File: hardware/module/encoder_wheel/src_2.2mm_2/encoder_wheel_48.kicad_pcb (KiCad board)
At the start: 2 copper layers, 74 x 74 mm, 2 parts

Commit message: encoder changes
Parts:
- renumbered REF** to ENC1, REF** to ENC2

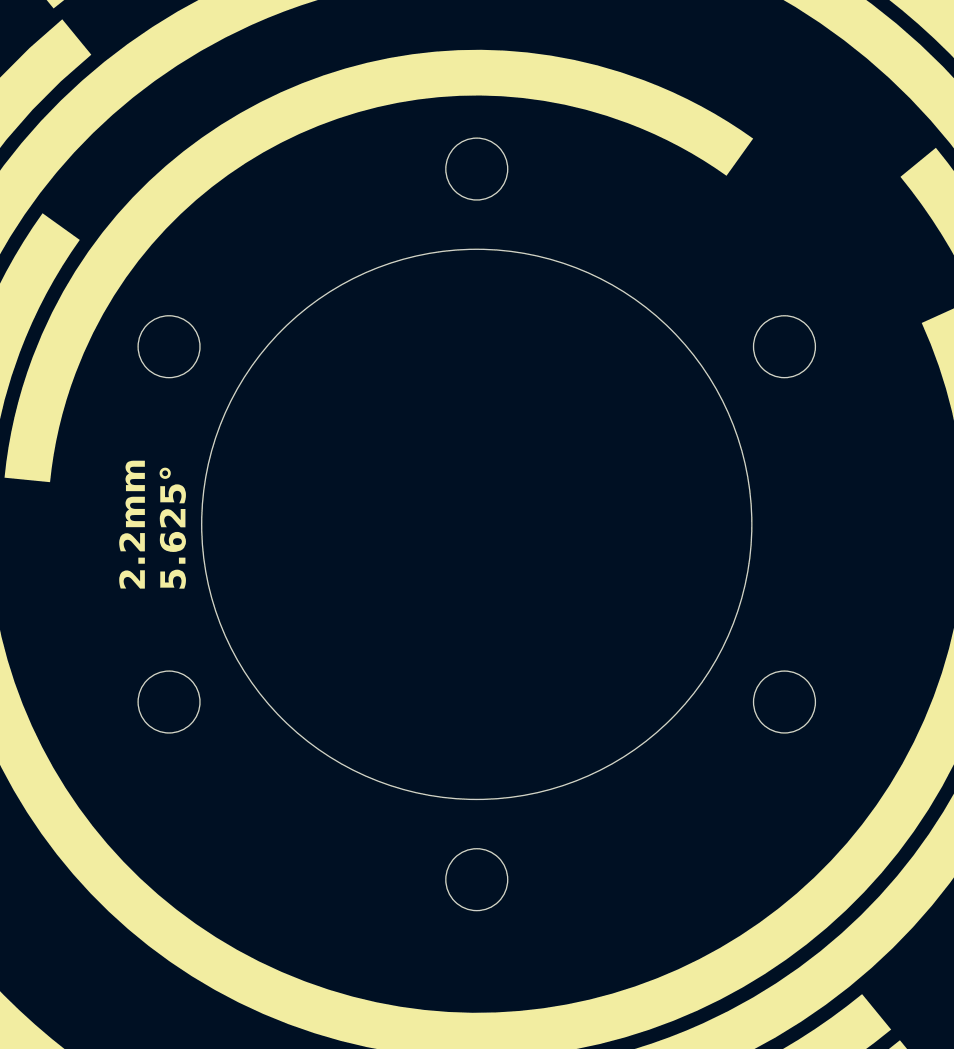
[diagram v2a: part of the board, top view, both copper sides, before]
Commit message: changed hole patern encoder wheel
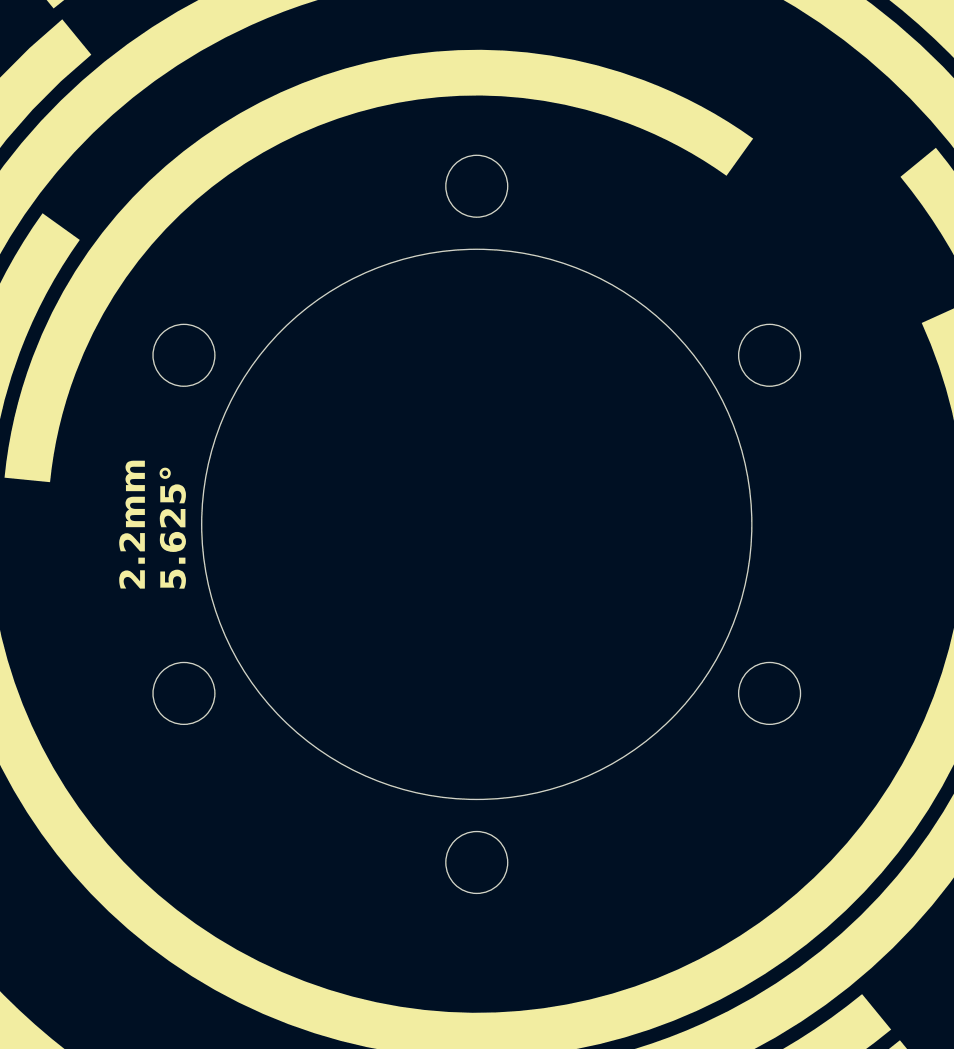
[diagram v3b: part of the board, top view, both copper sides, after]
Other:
- outline, holes or cut-outs redrawn
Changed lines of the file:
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@@
 				(xy 15.411921 -29.970747) (xy 15.898127 -29.716055) (xy 16.378717 -29.454359) (xy 16.853678 -29.185778)
 				(xy 15.852625 -27.453656) (xy 15.405903 -27.705999) (xy 14.953888 -27.951905) (xy 14.496592 -28.191261)
-				(xy 14.034024 -28.423958) (xy 13.566196 -28.649886) (xy 13.093119 -28.868934) (xy 12.6148 -29.080992)
+				(xy 14.034024 -28.423958) (xy 13.566196 -28.649886) (xy 13.093119 -28.868934) (xy 12.614798 -29.080992)
 				(xy 12.131258 -29.28595) (xy 11.645881 -29.482376) (xy 11.159155 -29.670143) (xy 10.671175 -29.849318)
 				(xy 10.182037 -30.019967) (xy 9.691836 -30.182158) (xy 9.200669 -30.335958) (xy 8.708632 -30.481435)
@@
 				(xy 5.848459 25.233587) (xy 5.027658 25.410212) (xy 4.205519 25.559396) (xy 3.382624 25.681424)
 				(xy 3.121843 23.700253) (xy 3.880692 23.587004) (xy 4.638938 23.448764) (xy 5.396048 23.285271)
-				(xy 6.15149 23.096262) (xy 6.904733 22.881472) (xy 7.655243 22.640638) (xy 8.402493 22.373497) (xy 9.145941 22.079785)
+				(xy 6.15149 23.096262) (xy 6.904733 22.881472) (xy 7.655243 22.640638) (xy 8.402495 22.373497) (xy 9.145941 22.079785)
 				(xy 10.271285 21.58003) (xy 11.358193 21.030029) (xy 12.405858 20.431736) (xy 13.413469 19.787104)
 				(xy 14.380217 19.098086) (xy 15.305294 18.366635) (xy 16.187891 17.594705) (xy 17.027198 16.784249)
@@
 				(xy -22.883793 -4.400149) (xy -22.634455 -5.538097) (xy -22.325558 -6.67145) (xy -21.956306 -7.798286)
 				(xy -21.525904 -8.916684) (xy -21.215974 -9.631281) (xy -20.884991 -10.330217) (xy -20.533501 -11.013306)
-				(xy -20.162047 -11.680366) (xy -19.771177 -12.3312) (xy -19.361434 -12.965632) (xy -18.933364 -13.583472)
+				(xy -20.162047 -11.680367) (xy -19.771177 -12.3312) (xy -19.361434 -12.965632) (xy -18.933364 -13.583472)
 				(xy -18.487513 -14.184533)
 			)
@@
 		(fp_poly
 			(pts
-				(xy 32.816366 7.646893) (xy 33.049092 6.574799) (xy 33.247099 5.49443) (xy 33.41003 4.406632) (xy 33.53754 3.312247)
+				(xy 32.816366 7.646893) (xy 33.04909 6.574799) (xy 33.247099 5.49443) (xy 33.41003 4.406632) (xy 33.53754 3.312247)
 				(xy 33.629279 2.212122) (xy 33.6849 1.107101) (xy 33.704054 -0.001973) (xy 31.709173 -0.001256)
 				(xy 31.691908 1.042432) (xy 31.640268 2.082254) (xy 31.554595 3.117414) (xy 31.43522 4.147115) (xy 31.282476 5.170561)
@@
 				(xy -15.850977 27.457433) (xy -16.735616 26.928095) (xy -17.171709 26.652536) (xy -17.603515 26.369771)
 				(xy -18.030934 26.07984) (xy -18.453864 25.782782) (xy -18.872208 25.478638) (xy -19.285857 25.167448)
-				(xy -19.694718 24.849256) (xy -20.098686 24.524092) (xy -20.497661 24.192005) (xy -20.891543 23.853032)
-				(xy -21.28023 23.507215) (xy -21.66362 23.154591) (xy -22.041617 22.795203) (xy -22.41411 22.42909)
+				(xy -19.694718 24.849258) (xy -20.098686 24.524092) (xy -20.497661 24.192005) (xy -20.891543 23.853032)
+				(xy -21.28023 23.507215) (xy -21.66362 23.154591) (xy -22.041619 22.795203) (xy -22.41411 22.42909)
 				(xy -23.824335 23.839929) (xy -23.026291 24.610225) (xy -22.205279 25.351807) (xy -21.362162 26.064344)
 				(xy -20.497803 26.747507) (xy -19.613068 27.400964) (xy -18.708815 28.024385) (xy -17.785909 28.61744)
@@
 				(xy 28.191978 -14.496459) (xy 28.424587 -14.033854) (xy 28.650427 -13.565988) (xy 28.869397 -13.092878)
 				(xy 29.0814 -12.614538) (xy 29.286337 -12.130986) (xy 29.482781 -11.645619) (xy 29.670599 -11.158915)
-				(xy 29.849849 -10.670966) (xy 30.020584 -10.181863) (xy 30.182862 -9.691701) (xy 30.336737 -9.200562)
+				(xy 29.849849 -10.670966) (xy 30.020584 -10.181863) (xy 30.182862 -9.691703) (xy 30.336737 -9.200562)
 				(xy 30.482266 -8.708546) (xy 30.619505 -8.215741)
 			)
@@
 				(xy 6.61534 -28.344697) (xy 7.538427 -28.112729) (xy 8.452701 -27.851011) (xy 9.357416 -27.559854)
 				(xy 10.251823 -27.239567) (xy 11.135173 -26.890462) (xy 12.006717 -26.512849) (xy 12.865706 -26.107039)
-				(xy 13.7114 -25.673343) (xy 14.543036 -25.212072) (xy 15.359876 -24.723536) (xy 16.161168 -24.208046)
+				(xy 13.711402 -25.673343) (xy 14.543036 -25.212072) (xy 15.359876 -24.723536) (xy 16.161168 -24.208046)
 				(xy 16.946165 -23.665913) (xy 17.714117 -23.097447)
 			)
@@
 				(xy -26.271921 3.515133) (xy -26.446168 1.791525) (xy -26.506944 0.05221) (xy -26.452039 -1.697465)
 				(xy -26.279238 -3.452157) (xy -28.259909 -3.712674) (xy -28.443963 -1.82717) (xy -28.501396 0.0533)
-				(xy -28.434604 1.922954) (xy -28.245982 3.776009) (xy -27.937924 5.60668) (xy -27.512827 7.409182)
+				(xy -28.434604 1.922954) (xy -28.245982 3.776009) (xy -27.937924 5.60668) (xy -27.512827 7.40918)
 				(xy -26.973085 9.17774) (xy -26.321094 10.906562) (xy -25.559248 12.589868) (xy -24.689943 14.221874)
 				(xy -23.715574 15.796796) (xy -22.638537 17.308852) (xy -21.461227 18.752259) (xy -20.186038 20.121232)
@@
 			(pts
 				(xy -22.516298 -18.44813) (xy -21.916483 -19.157491) (xy -21.292832 -19.848781) (xy -20.645625 -20.521316)
-				(xy -19.97514 -21.174415) (xy -19.281664 -21.807396) (xy -18.56547 -22.419576) (xy -17.826841 -23.010275)
+				(xy -19.975138 -21.174415) (xy -19.281664 -21.807396) (xy -18.56547 -22.419576) (xy -17.826841 -23.010275)
 				(xy -17.066057 -23.578808) (xy -16.283398 -24.124495) (xy -15.479145 -24.646653) (xy -14.653577 -25.144599)
 				(xy -13.806974 -25.617653) (xy -12.939618 -26.065132) (xy -12.051787 -26.486353) (xy -11.143763 -26.880635)
@@
 				(xy -15.359485 24.723954) (xy -16.160802 24.208466) (xy -16.945818 23.666331) (xy -17.713785 23.097858)
 				(xy -18.925882 24.677776) (xy -18.105156 25.284489) (xy -17.266224 25.863168) (xy -16.409889 26.41348)
-				(xy -15.536956 26.93509) (xy -14.648229 27.427666) (xy -13.744511 27.890865) (xy -12.826607 28.324362)
+				(xy -15.536956 26.93509) (xy -14.648229 27.427667) (xy -13.744511 27.890865) (xy -12.826607 28.324362)
 				(xy -11.895322 28.727819) (xy -10.951458 29.100903) (xy -9.995821 29.443278) (xy -9.029214 29.754612)
 				(xy -8.052442 30.034568) (xy -7.066308 30.282813) (xy -6.071617 30.499012) (xy -5.069172 30.682832)
@@
 				(xy -19.299668 17.27589) (xy -18.438653 18.193877) (xy -17.530045 19.072148) (xy -16.574728 19.908572)
 				(xy -15.573587 20.701017) (xy -14.527505 21.447352) (xy -13.437367 22.145446) (xy -12.304057 22.793166)
-				(xy -11.128458 23.388385) (xy -9.911455 23.928962) (xy -9.10605 24.247099) (xy -8.29639 24.536374)
+				(xy -11.128458 23.388387) (xy -9.911455 23.928962) (xy -9.10605 24.247099) (xy -8.29639 24.536374)
 				(xy -7.483058 24.797069) (xy -6.666635 25.029467) (xy -5.847704 25.233848) (xy -5.026848 25.410496)
 				(xy -4.204647 25.559691) (xy -3.381685 25.681716)
@@
 				(xy -0.194282 -28.503876) (xy -1.578992 -28.459321) (xy -2.955206 -28.34776) (xy -4.320573 -28.170168)
 				(xy -5.672745 -27.927516) (xy -7.009374 -27.620779) (xy -8.328108 -27.250928) (xy -9.626601 -26.818937)
-				(xy -10.902502 -26.32578) (xy -10.141516 -24.488598) (xy -10.141518 -24.488597) (xy -10.141523 -24.488596)
+				(xy -10.902502 -26.32578) (xy -10.141516 -24.488598) (xy -10.141518 -24.488597) (xy -10.141525 -24.488596)
 				(xy -10.141522 -24.488594) (xy -10.141524 -24.488593) (xy -10.141525 -24.488591) (xy -10.141527 -24.488589)
 				(xy -10.141529 -24.488588) (xy -10.14153 -24.488586) (xy -10.141531 -24.488584) (xy -10.141533 -24.488582)
@@
 				(xy 5.848459 -25.233587) (xy 5.027658 -25.410212) (xy 4.205519 -25.559396) (xy 3.382624 -25.681424)
 				(xy 3.121843 -23.700253) (xy 3.880692 -23.587004) (xy 4.638938 -23.448764) (xy 5.396048 -23.285271)
-				(xy 6.15149 -23.096262) (xy 6.904733 -22.881475) (xy 7.655243 -22.640638) (xy 8.40249 -22.373497)
+				(xy 6.15149 -23.096262) (xy 6.904733 -22.881477) (xy 7.655243 -22.640638) (xy 8.40249 -22.373497)
 				(xy 9.145941 -22.079785) (xy 10.271285 -21.58003) (xy 11.358193 -21.030029) (xy 12.405858 -20.431736)
 				(xy 13.413469 -19.787104) (xy 14.380217 -19.098086) (xy 15.305294 -18.366635) (xy 16.187891 -17.594705)
@@
 				(xy -16.455691 8.888347) (xy -16.886099 8.037721) (xy -17.277207 7.157007) (xy -17.506824 6.575849)
 				(xy -17.715691 5.991735) (xy -17.904014 5.405079) (xy -18.071999 4.816298) (xy -18.219853 4.225809)
-				(xy -18.347784 3.634028) (xy -18.455998 3.041372) (xy -18.544703 2.448257) (xy -20.523345 2.709613)
-				(xy -20.523346 2.709613) (xy -20.523347 2.709613) (xy -20.523348 2.709613) (xy -20.523351 2.709614)
+				(xy -18.347784 3.634028) (xy -18.455998 3.041372) (xy -18.544703 2.448257) (xy -20.523344 2.709613)
+				(xy -20.523344 2.709613) (xy -20.523345 2.709613) (xy -20.523346 2.709613) (xy -20.523351 2.709614)
 				(xy -20.523352 2.709614) (xy -20.523355 2.709615) (xy -20.523356 2.709615) (xy -20.523357 2.709615)
 				(xy -20.523358 2.709615) (xy -20.523359 2.709615) (xy -20.52336 2.709615) (xy -20.52336 2.709614)
@@
 	)
 	(gr_circle
-		(center 87.576606 107.75)
-		(end 88.926606 107.75)
+		(center 88.226125 107.375)
+		(end 89.576125 107.375)
 		(stroke
 			(width 0.05)
@@
 	)
 	(gr_circle
-		(center 101 84.5)
-		(end 102.35 84.5)
+		(center 101 85.25)
+		(end 102.35 85.25)
 		(stroke
 			(width 0.05)
@@
 	)
 	(gr_circle
-		(center 114.423394 92.25)
-		(end 115.773394 92.25)
+		(center 113.773875 92.625)
+		(end 115.123875 92.625)
 		(stroke
 			(width 0.05)
@@
 	)
 	(gr_circle
-		(center 87.576606 92.25)
-		(end 88.926606 92.25)
+		(center 88.226125 92.625)
+		(end 89.576125 92.625)
 		(stroke
 			(width 0.05)
@@
 	)
 	(gr_circle
-		(center 114.423394 107.75)
-		(end 115.773394 107.75)
+		(center 113.773875 107.375)
+		(end 115.123875 107.375)
 		(stroke
 			(width 0.05)
@@
 	)
 	(gr_circle
-		(center 101 115.5)
-		(end 102.35 115.5)
+		(center 101 114.75)
+		(end 102.35 114.75)
 		(stroke
 			(width 0.05)
